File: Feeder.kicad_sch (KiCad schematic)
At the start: 33 parts, among them J101 Conn_02x03_Odd_Even, J102 Conn_01x03_Pin, J103 Conn_01x02_Pin, U101 XBLW 24C02S(XBLW)

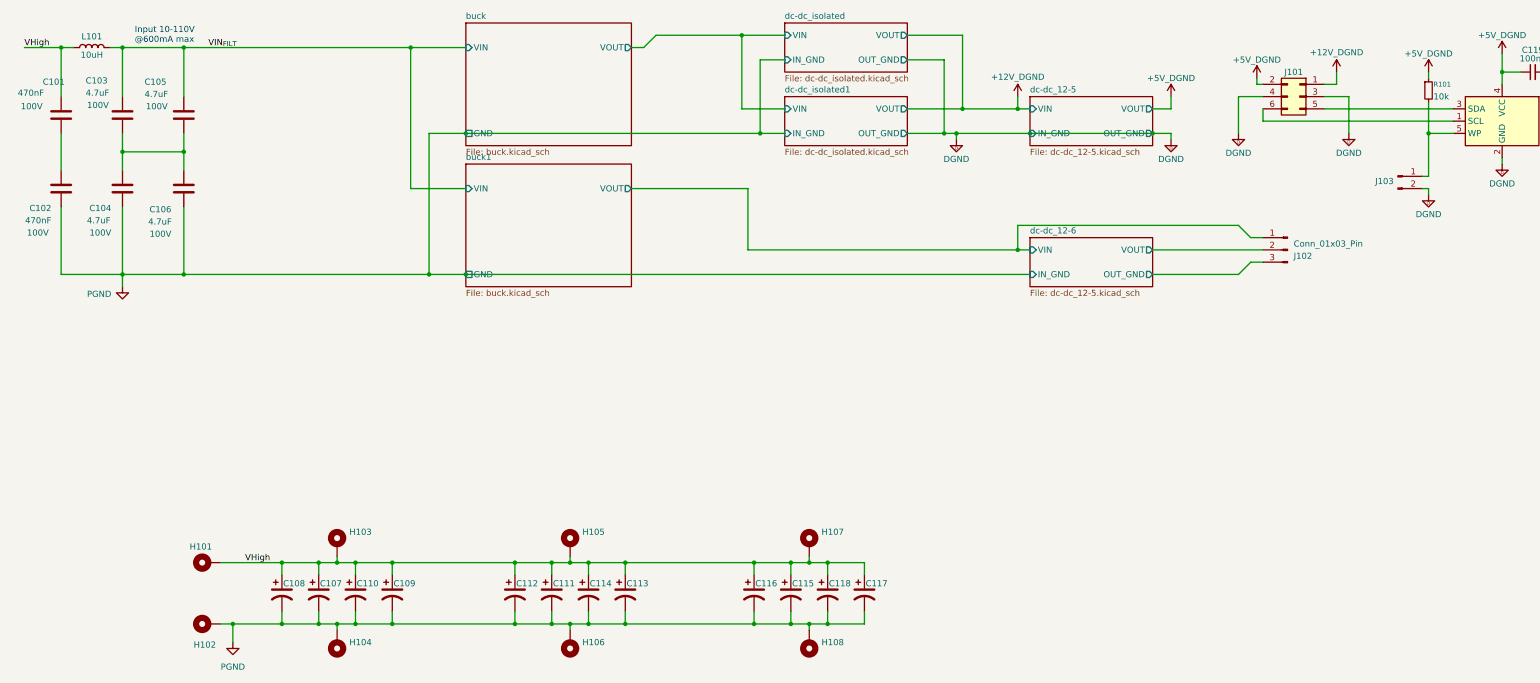
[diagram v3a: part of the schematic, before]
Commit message: feeder is routed
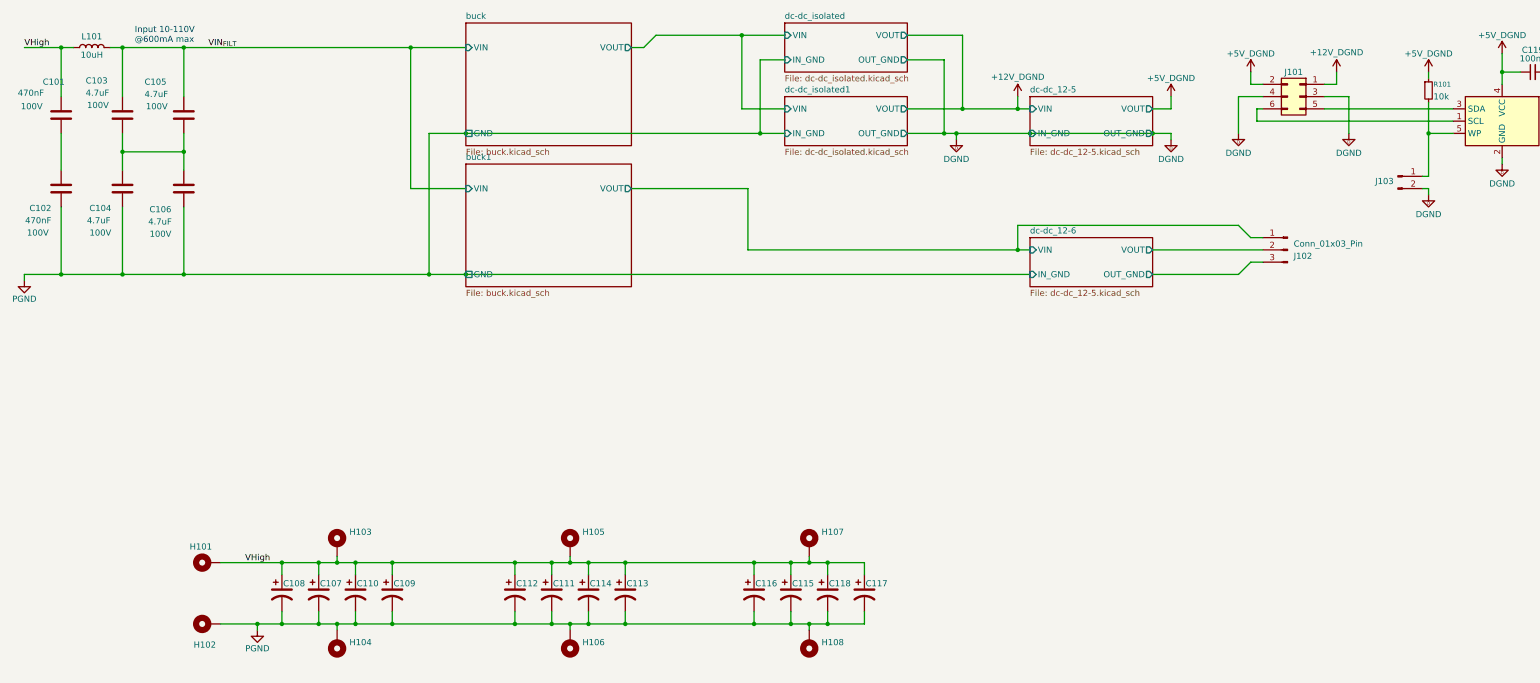
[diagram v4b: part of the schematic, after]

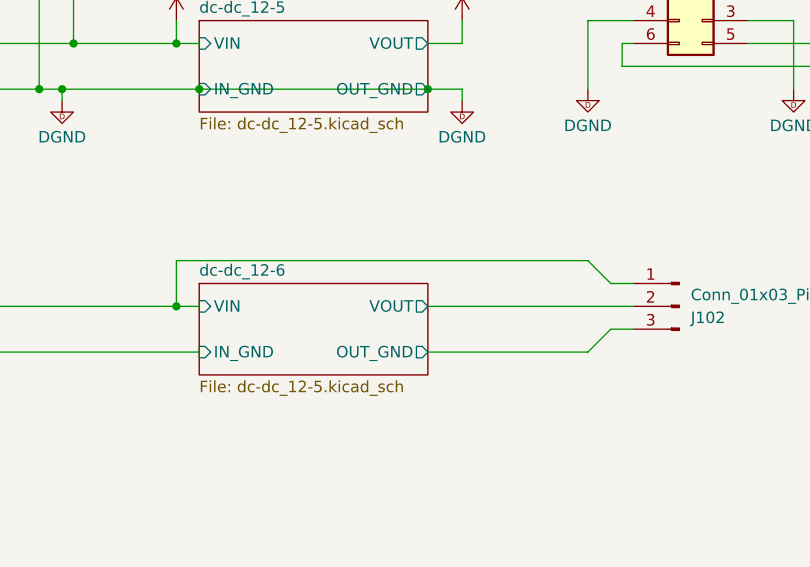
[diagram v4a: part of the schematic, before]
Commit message: routing is done but violations are still present
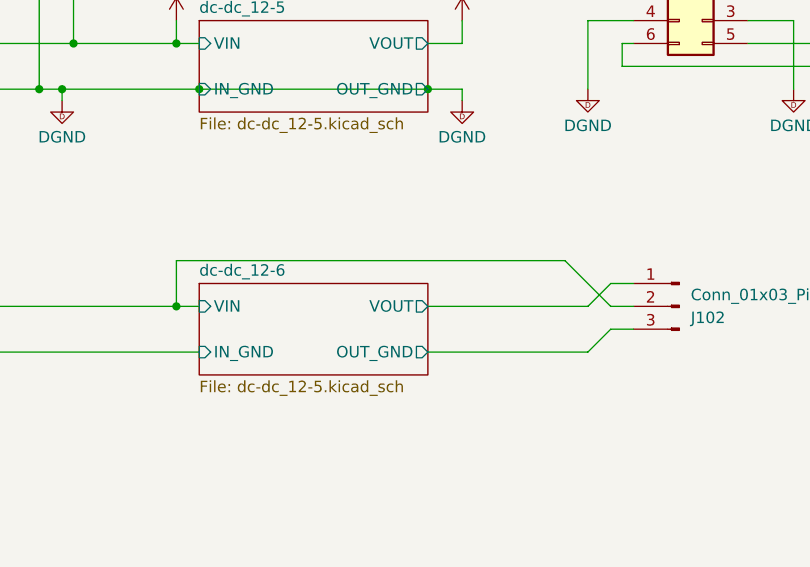
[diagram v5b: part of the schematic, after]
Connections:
- net buck1/VOUT: now also J102.2 (Pin_2); no longer J102.1 (Pin_1)
- net dc-dc_12-6/VOUT: now also J102.1 (Pin_1); no longer J102.2 (Pin_2)

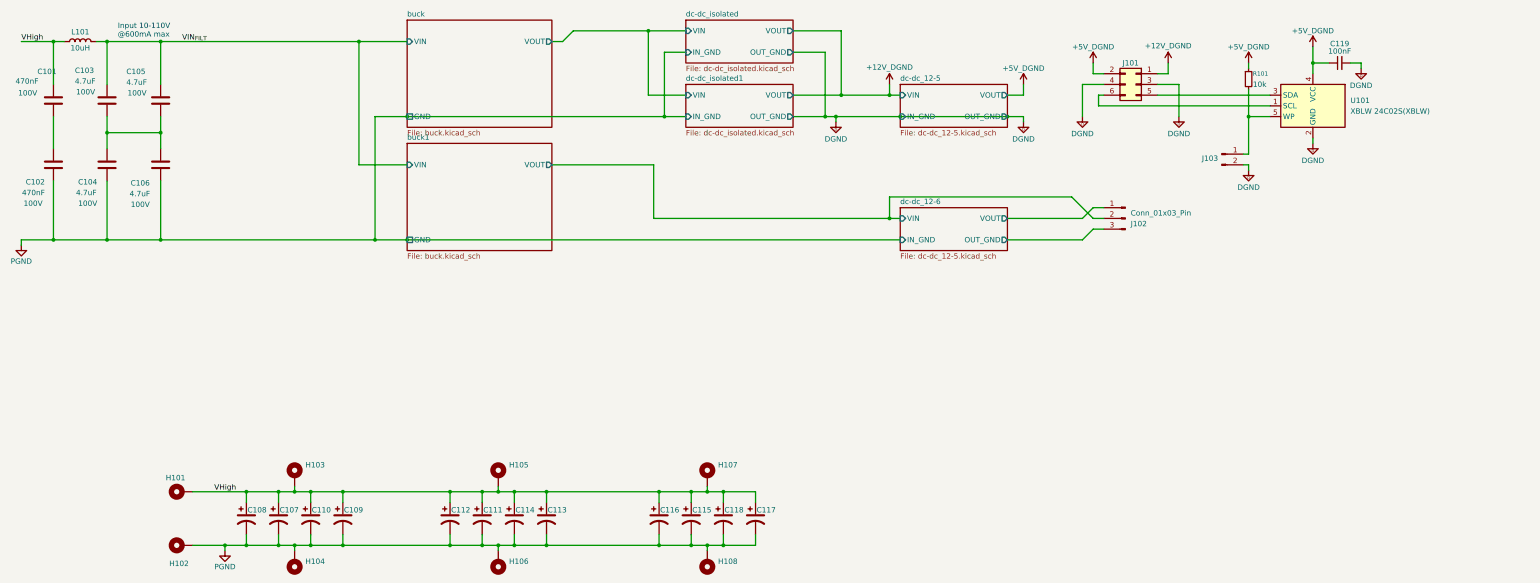
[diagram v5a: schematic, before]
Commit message: no erc errors
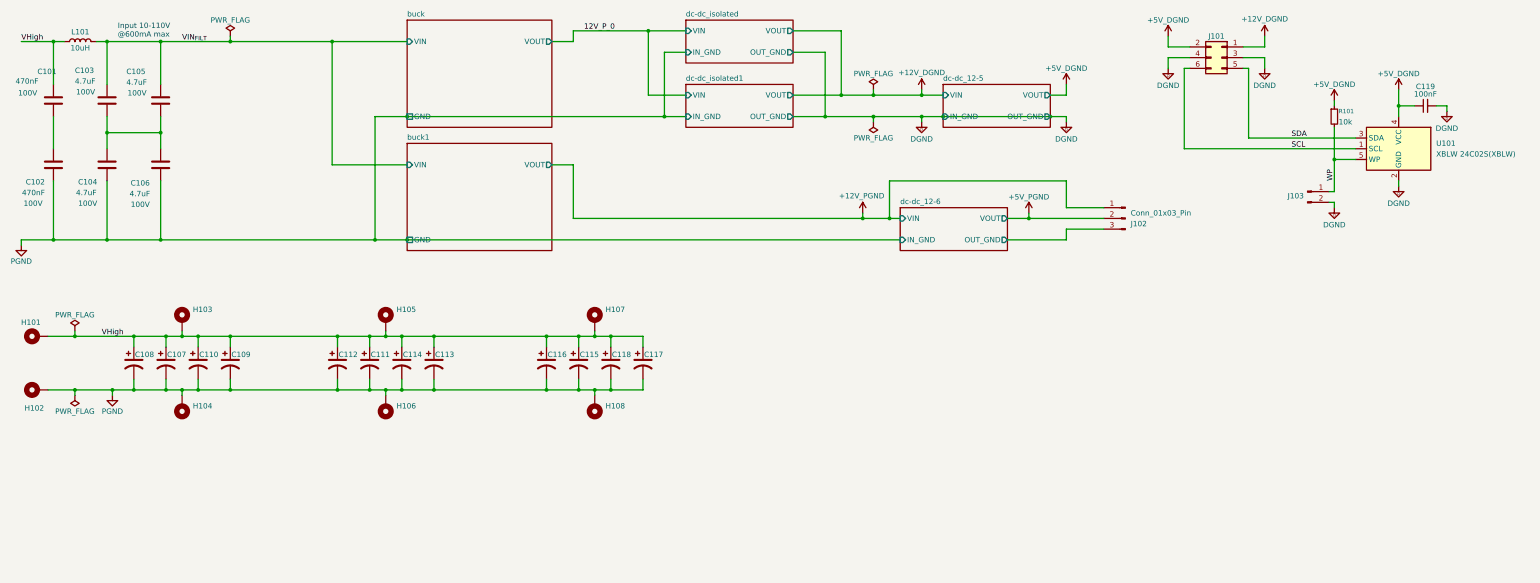
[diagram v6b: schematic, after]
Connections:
- net SCL: now reaches J101.6 (Pin_6), U101.1 (SCL)
- net SDA: now reaches J101.5 (Pin_5), U101.3 (SDA)
- net WP: now reaches J103.1 (Pin_1), R101.2, U101.5 (WP)
- net buck1/VOUT renamed +5V_PGND
- net dc-dc_12-6/VOUT renamed +12V_PGND
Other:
- moved on the sheet: C107, C108, C109, C110, C111, C112, C113, C114, C115, C116, C117, C118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

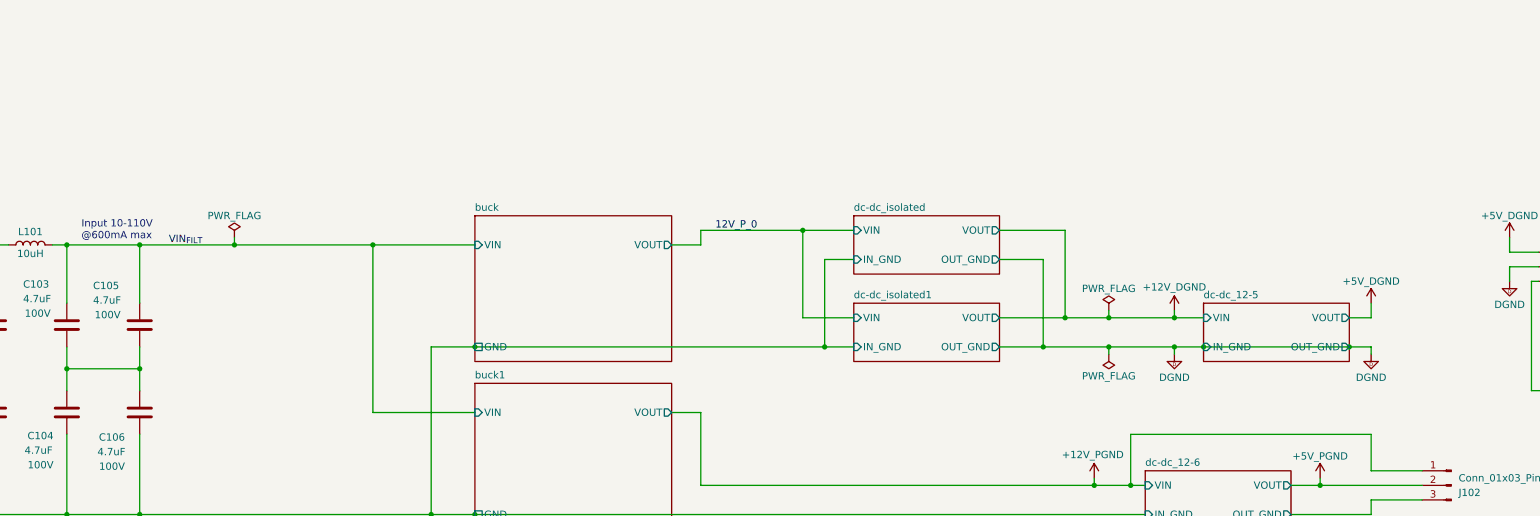
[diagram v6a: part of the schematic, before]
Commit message: added drawing to the schematic
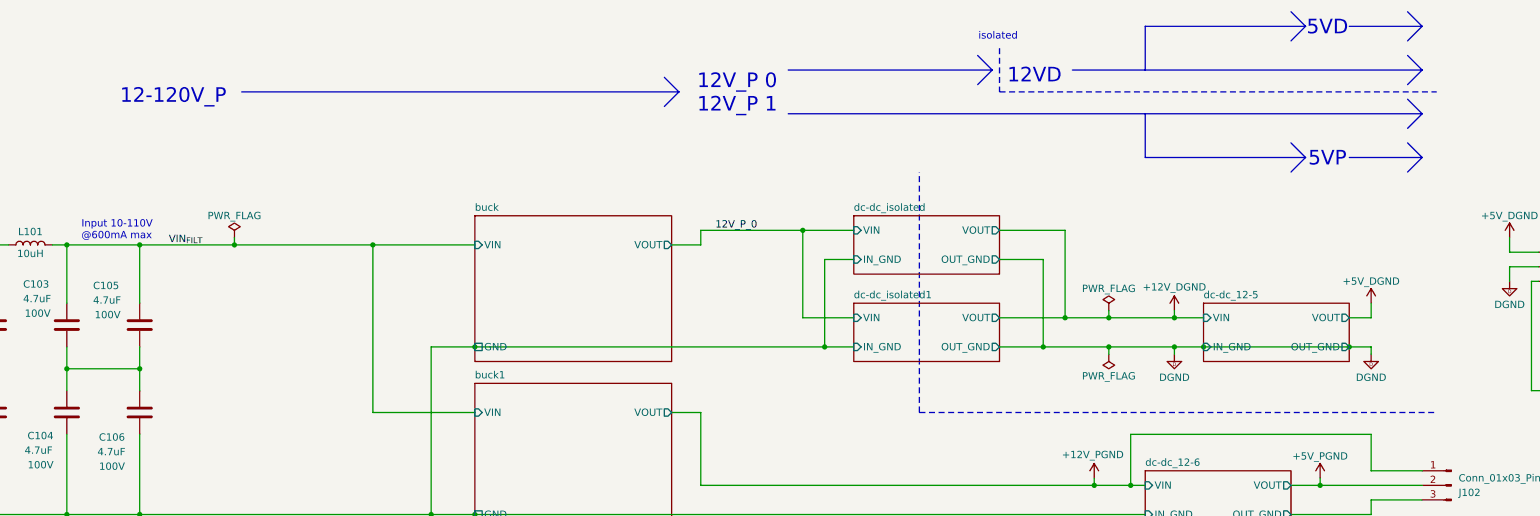
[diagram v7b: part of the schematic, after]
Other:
- note added: "12-120V_P"
- note added: "12VD"
- note added: "12V_P 0 12V_P 1"
- note added: "5VD"
- note added: "5VP"
- note added: "isolated"

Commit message: v2 wip
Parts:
- removed J103: Conn_01x02_Pin, Connector_PinHeader_2.54mm:PinHeader_1x02_P2.54mm_Vertical, symbol Connector:Conn_01x02_Pin
- removed R101: 10k, Capacitor_SMD:C_0603_1608Metric, symbol Device:R_Small
- added D101, D102, D103: LED, LED_SMD:LED_0402_1005Metric, symbol Device:LED
- added JP101, JP105: Jumper_3_Open, Connector_PinHeader_2.54mm:PinHeader_1x03_P2.54mm_Vertical, symbol Jumper:Jumper_3_Open
- added JP102, JP103, JP104: Jumper_2_Bridged, Footprints:SolderJumper-2_P1.3mm_Bridged_RoundedPad1.0x1.5mm, symbol Jumper:Jumper_2_Bridged
- added R101: 22k, Footprints:R_0805_2012Metric, symbol Device:R
- added R107: 2k2, Resistor_SMD:R_0402_1005Metric, symbol Device:R_Small
- added R110, R111: 1k, Resistor_SMD:R_0402_1005Metric, symbol Device:R_Small
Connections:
- net WP is gone; now on net DGND: U101.5 (WP)
- net dc-dc_12-6/OUT_GND is gone; now on net PGND: J102.3 (Pin_3)
- net +12V_DGND: now also JP101.2 (C)
- net +12V_PGND: now also JP102.1 (A), R101.1
- net PGND: now also D102.1 (K), D103.1 (K), JP105.1 (A)
- new net: JP102.2 (B), R107.2
- new net: D101.2 (A), R107.1
- new net: JP103.2 (B), R110.2
- new net: D102.2 (A), R110.1
- new net: D103.2 (A), R111.1
- new net: JP104.2 (B), R111.2
- new net 12V_DIGI_TO_POWER: JP104.1 (A)
- new net 12V_PWR_BUS: JP103.1 (A)
- new net buck/~{EN}: D101.1 (K), JP105.2 (C), JP105.3 (B), R101.2
- new net dc-dc_isolated/VIN: JP101.1 (A)
- new net dc-dc_isolated_disabling/VOUT: JP101.3 (B)
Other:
- removed sheet dc-dc_isolated1
- added sheet Ideal Diolde (ideal_diode.kicad_sch)
- added sheet dc-dc_isolated_disabling (dc-dc_isolated_disabling.kicad_sch)
- added sheet dc-dc_isolated_disabling1 (dc-dc_isolated_disabling.kicad_sch)
- sheet buck ports: added ~{EN}; removed none
- sheet buck1 ports: added ~{EN}; removed none
- note added: "12-120V Bus supply"
- note added: "12V in"
- note added: "12VP"
- note added: "<- Always on if the jumper is from external"
- note added: "BUS supply"
- note added: "External supply mode"
- note added: "Lights up when <- ~{EN} is LOW (enabled)"
- note added: "Select if the supply is coming either from the high side or the board."
- moved on the sheet: C107, C108, C109, C110, C111, C112, C113, C114, C115, C116, C117, C118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
